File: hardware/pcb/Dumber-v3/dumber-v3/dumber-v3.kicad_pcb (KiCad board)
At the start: 2 copper layers, 88 x 86 mm, 69 parts, among them J1 Conn_02x03_Odd_Even, J2 Conn_02x03_Odd_Even, J3 Conn_02x05_Odd_Even, J4 TE 1-84982-0, M1 Motor, M2 Motor, P1 USB_C_Plug_GCT_USB4125, Q1 PMN52XP, Q2 PMN52XP, SW1 SW_Push, U1 XBEE-3, U2 STM32F071CBTx, U3 LTC2954-2, U4 L6924U, U5 LM2731XMF, U6 AP2206, U7 A3909

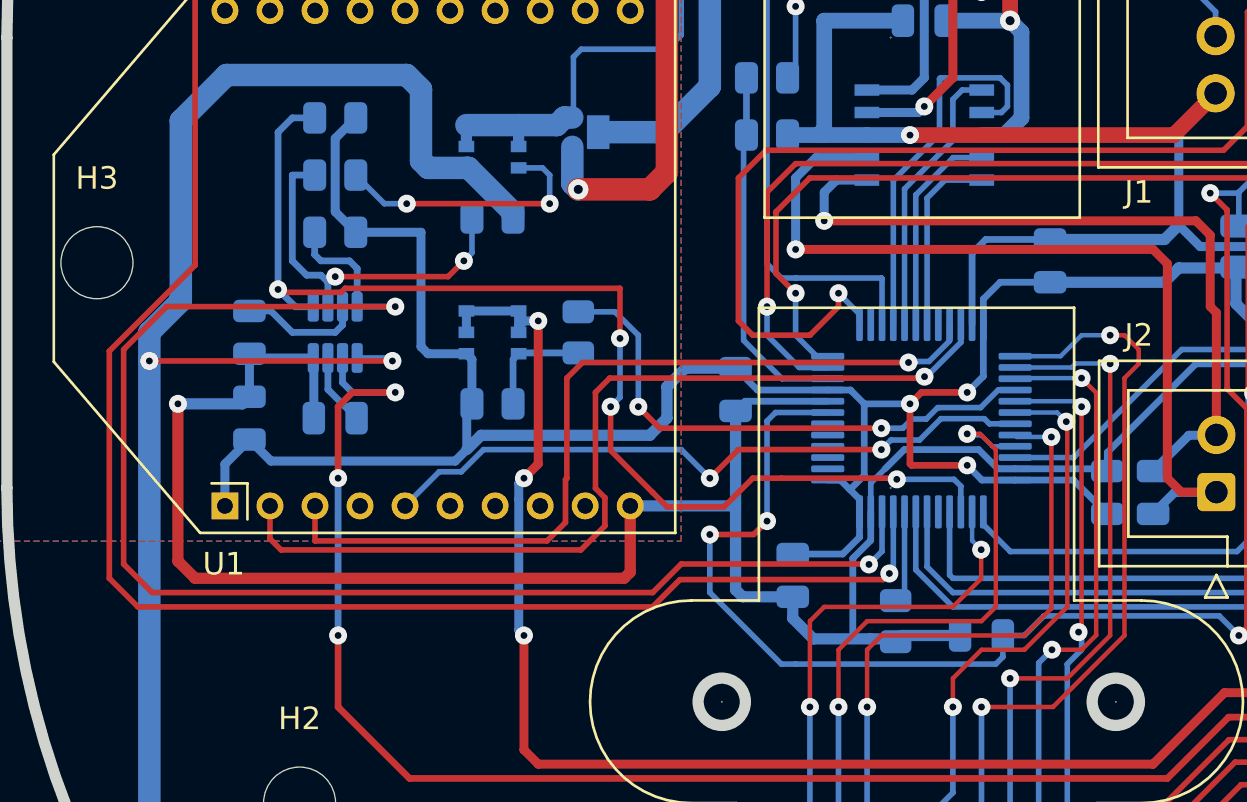
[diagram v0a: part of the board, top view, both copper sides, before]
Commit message: Modifications after testing: func 11 needs more work.
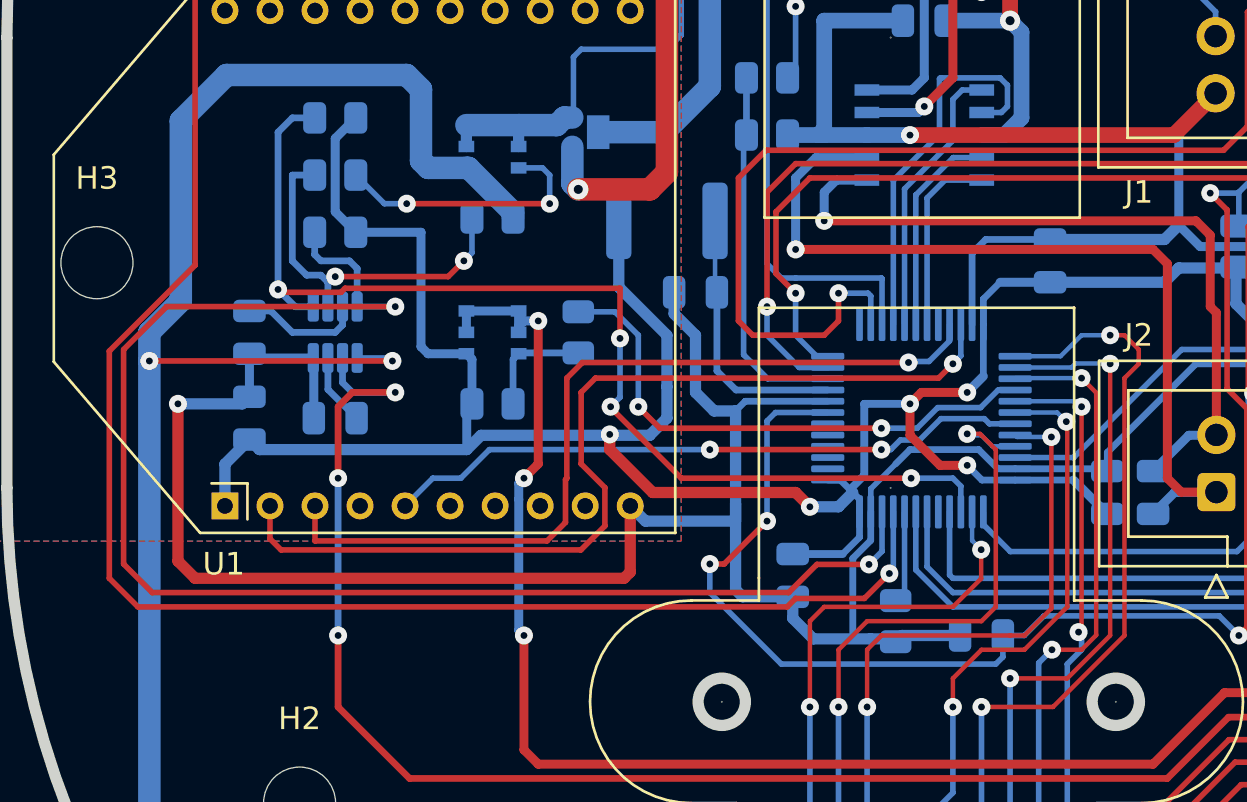
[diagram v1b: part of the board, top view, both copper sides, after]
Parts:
- removed C20: 100nF, Capacitor_SMD:C_0805_2012Metric
- added C22: 1µF, Capacitor_SMD:C_0805_2012Metric, B.Cu at (140.3, 107.3)
- added L2: 5,6µH, Inductor_SMD:L_1812_4532Metric, B.Cu at (139.1, 104.1)
- C11, C6: value 1µF -> 10µF
- R17: value 150K -> 1K
- R18: value 100K -> 1K
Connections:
- U2 pad 13: /Cpu/ENCDROIT_B -> unconnected-(U2-Pad13)
- U2 pad 14: unconnected-(U2-Pad14) -> /Cpu/ENCDROIT_B
- U2 pad 9: +2V5 -> Net-(U2-Pad9)
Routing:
- net Net-(U2-Pad9): track 0.00 -> 12.0 mm
- net +2V5: track 163.1 -> 173.2 mm, vias 6 -> 8
- net GND: track 361.2 -> 369.1 mm
- net /Cpu/BUTTON_SENSE: track 51.9 -> 49.7 mm
- net /Cpu/ENCDROIT_B: track 70.3 -> 71.6 mm
- net /Cpu/USART_RX: track 41.0 -> 42.3 mm
- net /Cpu/XBEE_RESET: track 29.8 -> 28.8 mm
- net /Cpu/RESET: track 96.0 -> 95.2 mm
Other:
- board text added: "Dumber 3 V2.2 INSA-GEI 03/23"
- board text removed: "Dumber 3 V2.1 INSA-GEI 01/23"
